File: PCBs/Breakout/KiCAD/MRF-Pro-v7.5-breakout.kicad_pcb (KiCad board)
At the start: 2 copper layers, 21 x 15.5 mm, 5 parts, among them J5 FPC 8P Connector, J6 Stemma QT, J7 TFS20L / DTS6012M

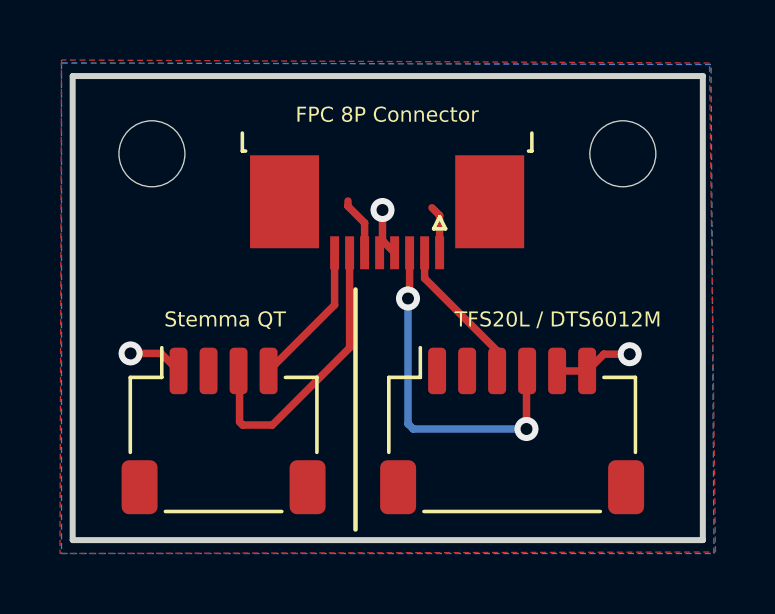
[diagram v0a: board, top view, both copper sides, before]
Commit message: Lay out LiDAR decoupling caps on the breakout board
Place and route C1/C2/C3 across the LiDAR 3.3V rail at J7. DRC is clean
apart from a known-benign courtyard touch between the bulk cap and the
mounting hole. Schematic re-saved in KiCad's canonical format (caps and
connectivity unchanged, ERC clean).

Completes stage 1 of the breakout respin; boards ordered for field testing.
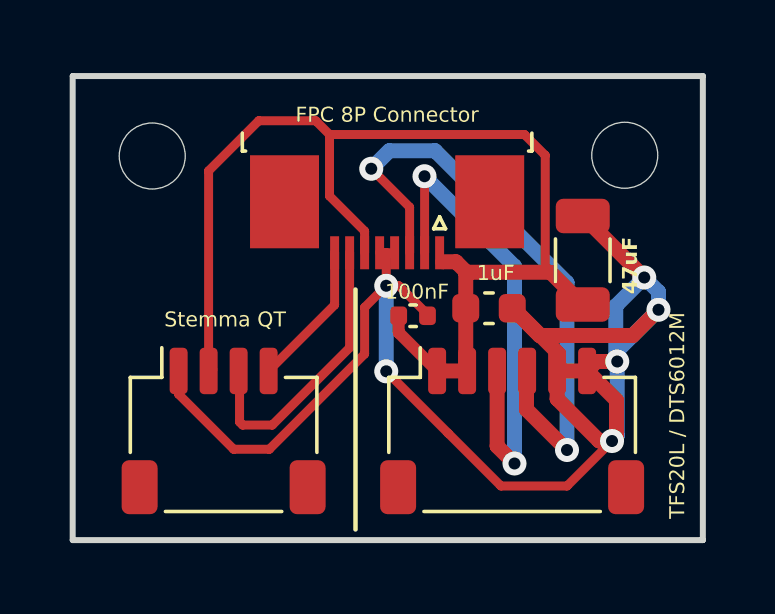
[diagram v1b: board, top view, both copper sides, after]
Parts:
- removed the REF** at (120.0, 125.5)
- removed the REF** at (135.7, 125.5)
- added C1: 47uF, Capacitor_SMD:C_1206_3216Metric, F.Cu at (134.3, 129.0)
- added C2: 1uF, Capacitor_SMD:C_0603_1608Metric, F.Cu at (131.2, 130.6)
- added C3: 100nF, Capacitor_SMD:C_0402_1005Metric, F.Cu at (128.7, 130.9)
- added REF**: MountingHole_2.2mm_M2, MountingHole:MountingHole_2.2mm_M2, F.Cu at (120.0, 125.5)
- added REF**: MountingHole_2.2mm_M2, MountingHole:MountingHole_2.2mm_M2, F.Cu at (135.7, 125.5)
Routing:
- net /GND: track 6.53 -> 57.1 mm, vias 3 -> 6
- net /3.3V: track 3.80 -> 39.8 mm
- net Net-(J5-Pin_2): track 4.94 -> 16.7 mm, vias 0 -> 2
- net Net-(J5-Pin_3): track 12.1 -> 21.2 mm
- removed copper zone on F.Cu, net /3.3V
- removed copper zone on B.Cu, net /GND
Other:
- board text added: "MRF2 Breakout v2.5"
- board text removed: "MRF2 Breakout v2.0"
